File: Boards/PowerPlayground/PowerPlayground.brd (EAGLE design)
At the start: 62.2 x 31.8 mm, 21 parts

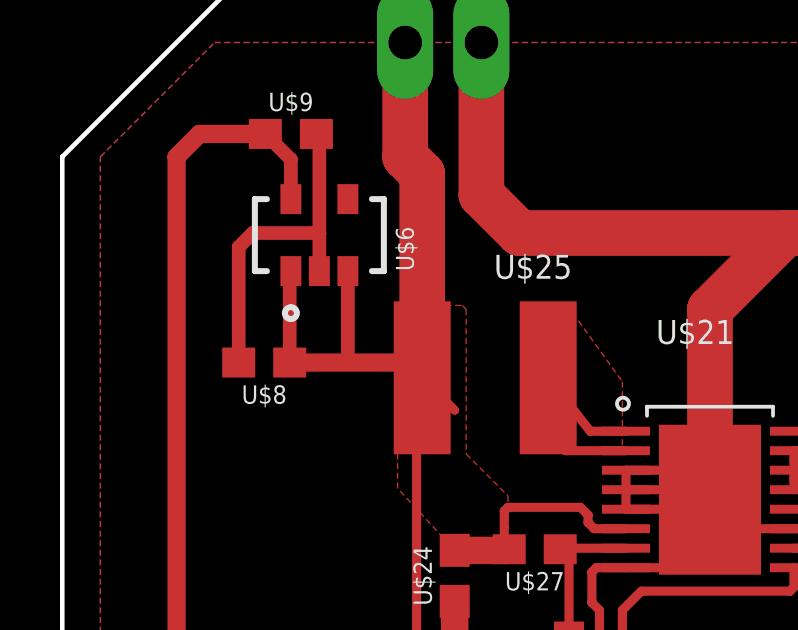
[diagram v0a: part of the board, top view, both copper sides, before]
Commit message: Added standoff part, switches, main board file, and others
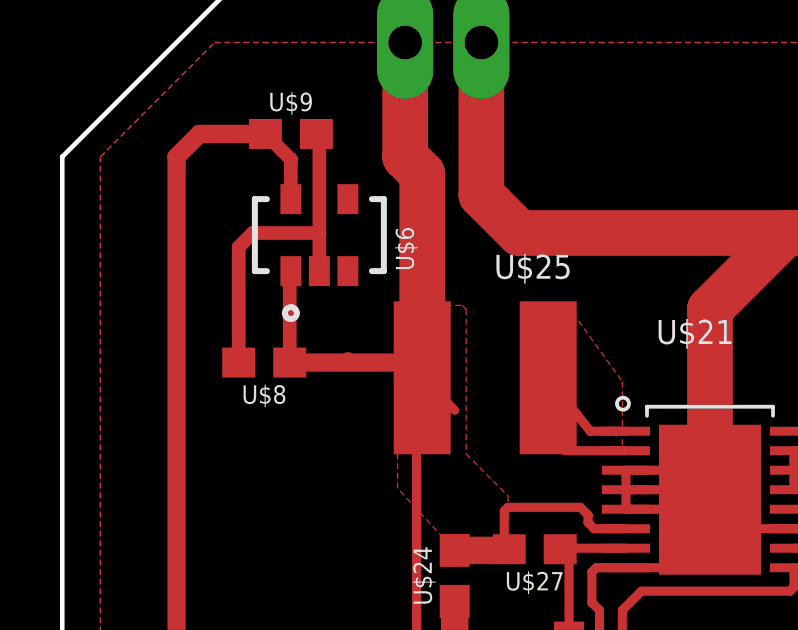
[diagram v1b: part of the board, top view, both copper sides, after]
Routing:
- net DB_V_BATT: track 61.8 -> 58.9 mm
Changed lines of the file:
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@@
 <contactref element="U$6" pad="PIN_1"/>
 <contactref element="U$8" pad="1"/>
-<contactref element="U$6" pad="PIN_3"/>
 <wire x1="13.931" y1="22.821" x2="13.931" y2="19.812" width="0.4572" layer="1"/>
 <wire x1="13.931" y1="22.821" x2="13.97" y2="22.86" width="0.4572" layer="1"/>
-<wire x1="15.87" y1="22.86" x2="15.87" y2="19.934" width="0.4572" layer="1"/>
 <wire x1="15.87" y1="19.934" x2="15.748" y2="19.812" width="0.4572" layer="1"/>
 <wire x1="15.748" y1="19.812" x2="13.931" y2="19.812" width="0.4572" layer="1"/>
@@
 <wire x1="13.931" y1="19.812" x2="17.839" y2="19.812" width="0.6096" layer="1"/>
 <wire x1="17.839" y1="19.812" x2="18.347" y2="19.304" width="0.6096" layer="1"/>
+<contactref element="U$6" pad="PIN_3"/>
+<wire x1="13.97" y1="22.86" x2="15.87" y2="22.86" width="0" layer="19" extent="1-1"/>
+<wire x1="25.1399875" y1="14.273290625" x2="25.654" y2="12.192" width="0" layer="19" extent="1-1"/>
 </signal>
 <signal name="VCC">
